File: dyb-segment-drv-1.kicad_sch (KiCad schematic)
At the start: 0 parts

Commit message: schem: add segment display
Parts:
- added U1: D168K, Display_7Segment:D1X8K, symbol Display_Character:D168K
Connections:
- new net: U1.3 (CA), U1.8 (CA)
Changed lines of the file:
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@@
 	(generator_version "10.0")
 	(paper "A4")
+	(symbol
+		(lib_id "Display_Character:D168K")
+		(at 48.26 45.72 0)
+		(unit 1)
+		(body_style 1)
+		(exclude_from_sim no)
+		(in_bom yes)
+		(on_board yes)
+		(in_pos_files yes)
+		(dnp no)
+		(fields_autoplaced yes)
+		(property "Reference" "U1"
+			(at 48.26 27.94 0)
+			(show_name no)
+			(do_not_autoplace no)
+			(effects
+				(font
+					(size 1.27 1.27)
+				)
+			)
+		)
+		(property "Value" "D168K"
+			(at 48.26 30.48 0)
+			(show_name no)
+			(do_not_autoplace no)
+			(effects
+				(font
+					(size 1.27 1.27)
+				)
+			)
+		)
+		(property "Footprint" "Display_7Segment:D1X8K"
+			(at 48.26 60.96 0)
+			(hide yes)
+			(show_name no)
+			(do_not_autoplace no)
+			(effects
+				(font
+					(size 1.27 1.27)
+				)
+			)
+		)
+		(property "Datasheet" "https://ia800903.us.archive.org/24/items/CTKD1x8K/Cromatek%20D168K.pdf"
+			(at 35.56 33.655 0)
+			(hide yes)
+			(show_name no)
+			(do_not_autoplace no)
+			(effects
+				(font
+					(size 1.27 1.27)
+				)
+				(justify left)
+			)
+		)
+		(property "Description" "One digit 7 segment ultra bright red LED, low current, common cathode"
+			(at 48.26 45.72 0)
+			(hide yes)
+			(show_name no)
+			(do_not_autoplace no)
+			(effects
+				(font
+					(size 1.27 1.27)
+				)
+			)
+		)
+		(pin "10"
+		)
+		(pin "9"
+		)
+		(pin "8"
+		)
+		(pin "7"
+		)
+		(pin "6"
+		)
+		(pin "1"
+		)
+		(pin "4"
+		)
+		(pin "5"
+		)
+		(pin "3"
+		)
+		(pin "2"
+		)
+		(instances
+			(project "dyb-segment-drv-1"
+				(path "/0d1f997b-7d97-47c3-85c1-1ce9346504d0"
+					(reference "U1")
+					(unit 1)
+				)
+			)
+		)
+	)
 	(sheet_instances
 		(path "/"

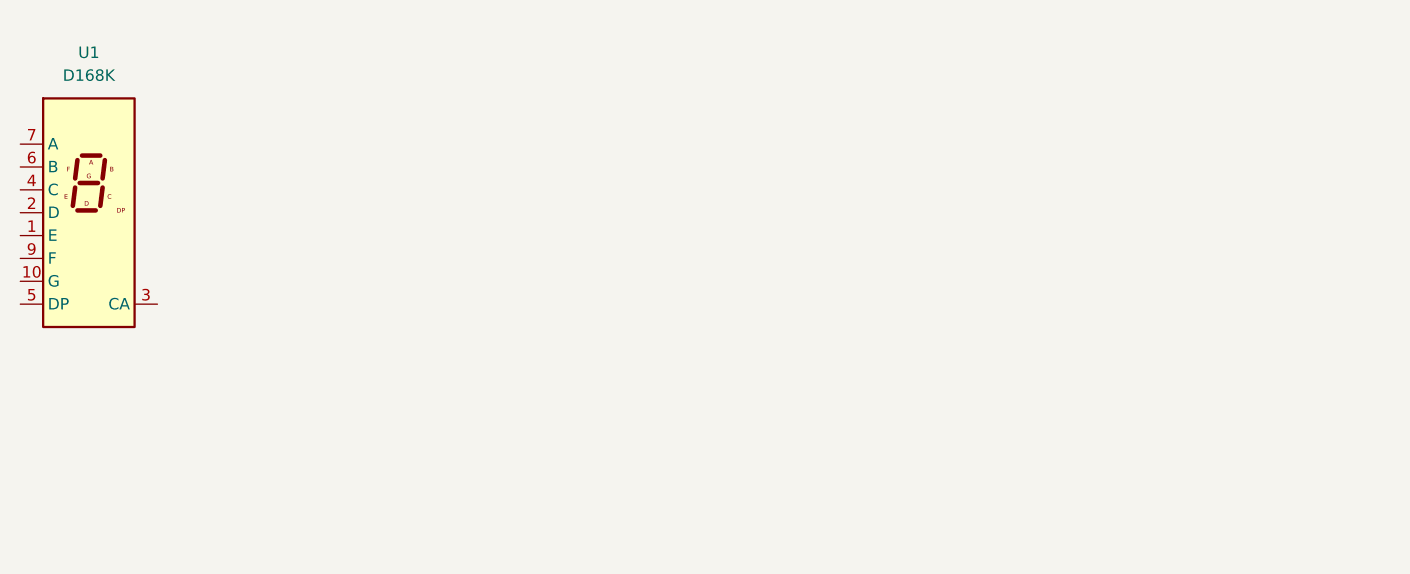
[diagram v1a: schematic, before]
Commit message: schem: add all logic gates
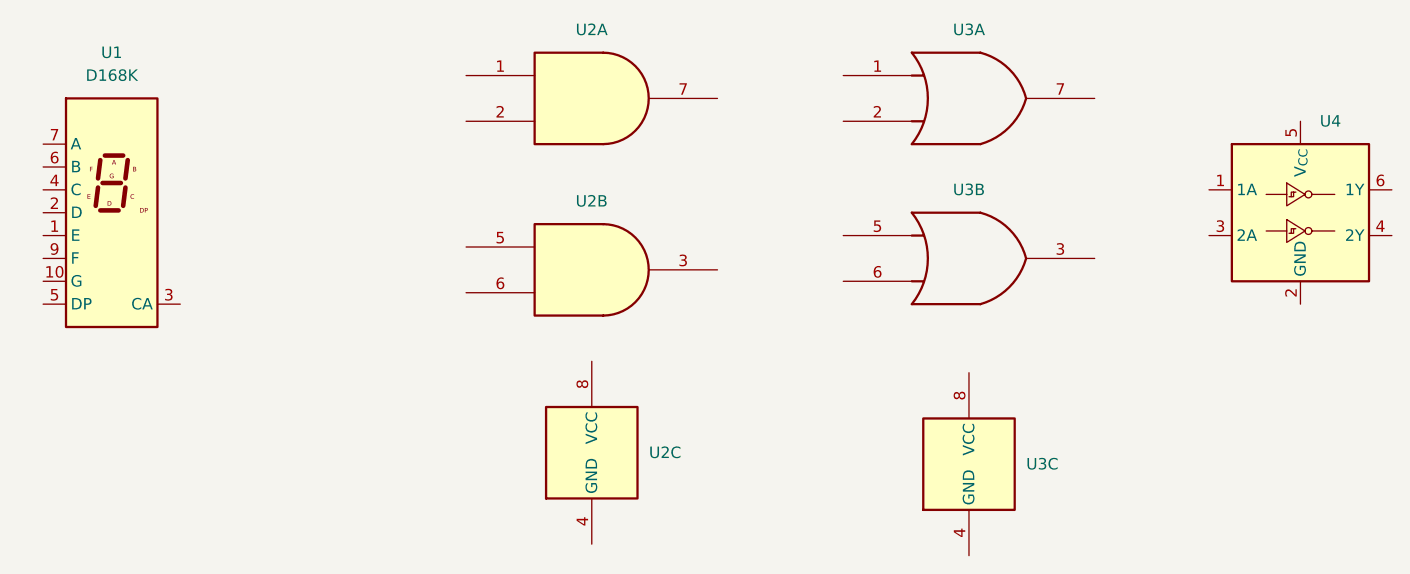
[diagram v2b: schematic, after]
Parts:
- added U2: SN74AUP2G08, Package_SO:VSSOP-8_2.3x2mm_P0.5mm, symbol GLCS:SN74AUP2G08
- added U3: 74AUC2G32, Package_DFN_QFN:QFN-20-1EP_5x5mm_P0.65mm_EP3.35x3.35mm, symbol 74xGxx:74AUC2G32
- added U4: Inverter_Schmitt_Dual, Package_TO_SOT_SMD:SOT-23-6, symbol 74xGxx:Inverter_Schmitt_Dual
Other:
- moved on the sheet: U1

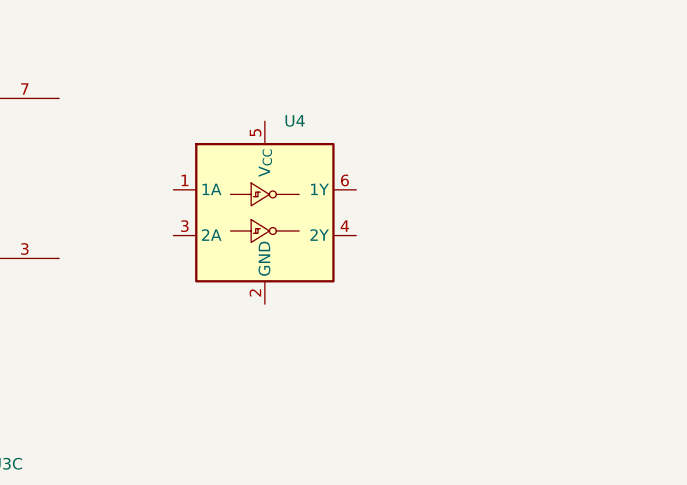
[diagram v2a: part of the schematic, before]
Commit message: schem: add mosfet
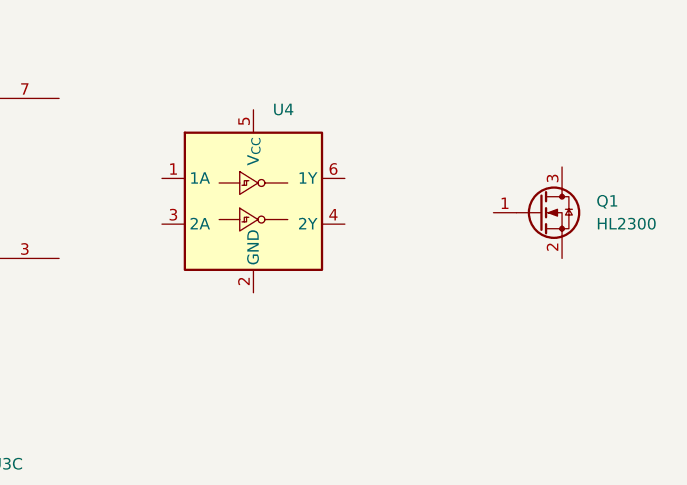
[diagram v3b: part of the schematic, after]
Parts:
- added Q1: HL2300, Package_TO_SOT_SMD:SOT-23, symbol Transistor_FET:DMN24H11DS
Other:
- moved on the sheet: U4
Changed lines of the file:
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@@
 	(symbol
 		(lib_id "74xGxx:Inverter_Schmitt_Dual")
-		(at 182.88 45.72 0)
+		(at 181.61 44.45 0)
 		(unit 1)
 		(body_style 1)
@@
 		(fields_autoplaced yes)
 		(property "Reference" "U4"
-			(at 185.0233 35.56 0)
+			(at 183.7533 34.29 0)
 			(show_name no)
 			(do_not_autoplace no)
@@
 		)
 		(property "Value" "Inverter_Schmitt_Dual"
-			(at 185.0233 35.56 0)
+			(at 183.7533 34.29 0)
 			(hide yes)
 			(show_name no)
@@
 		)
 		(property "Footprint" "Package_TO_SOT_SMD:SOT-23-6"
-			(at 182.88 45.72 0)
+			(at 181.61 44.45 0)
 			(hide yes)
 			(show_name no)
@@
 		)
 		(property "Datasheet" ""
-			(at 182.88 45.72 0)
+			(at 181.61 44.45 0)
 			(hide yes)
 			(show_name no)
@@
 		)
 		(property "Description" "Dual schmitt inverter"
-			(at 182.88 45.72 0)
+			(at 181.61 44.45 0)
 			(hide yes)
 			(show_name no)
@@
 					(unit 1)
 				)
+			)
+		)
+	)
+	(symbol
+		(lib_id "Transistor_FET:DMN24H11DS")
+		(at 213.36 45.72 0)
+		(unit 1)
+		(body_style 1)
+		(exclude_from_sim no)
+		(in_bom yes)
+		(on_board yes)
+		(in_pos_files yes)
+		(dnp no)
+		(fields_autoplaced yes)
+		(property "Reference" "Q1"
+			(at 219.71 44.4499 0)
+			(show_name no)
+			(do_not_autoplace no)
+			(effects
+				(font
+					(size 1.27 1.27)
+				)
+				(justify left)
+			)
+		)
+		(property "Value" "HL2300"
+			(at 219.71 46.9899 0)
+			(show_name no)
+			(do_not_autoplace no)
+			(effects
+				(font
+					(size 1.27 1.27)
+				)
+				(justify left)
+			)
+		)
+		(property "Footprint" "Package_TO_SOT_SMD:SOT-23"
+			(at 218.44 47.625 0)
+			(hide yes)
+			(show_name no)
+			(do_not_autoplace no)
+			(effects
+				(font
+					(size 1.27 1.27)
+					(italic yes)
+				)
+				(justify left)
+			)
+		)
+		(property "Datasheet" "http://www.diodes.com/assets/Datasheets/DMN24H11DS.pdf"
+			(at 218.44 49.53 0)
+			(hide yes)
+			(show_name no)
+			(do_not_autoplace no)
+			(effects
+				(font
+					(size 1.27 1.27)
+				)
+				(justify left)
+			)
+		)
+		(property "Description" "0.27A Id, 240V Vds, N-Channel MOSFET, SOT-23"
+			(at 213.36 45.72 0)
+			(hide yes)
+			(show_name no)
+			(do_not_autoplace no)
+			(effects
+				(font
+					(size 1.27 1.27)
+				)
+			)
+		)
+		(pin "1"
+		)
+		(pin "3"
+		)
+		(pin "2"
+		)
+		(instances
+			(project "dyb-segment-drv-1"
+				(path "/0d1f997b-7d97-47c3-85c1-1ce9346504d0"
+					(reference "Q1")
+					(unit 1)
+				)

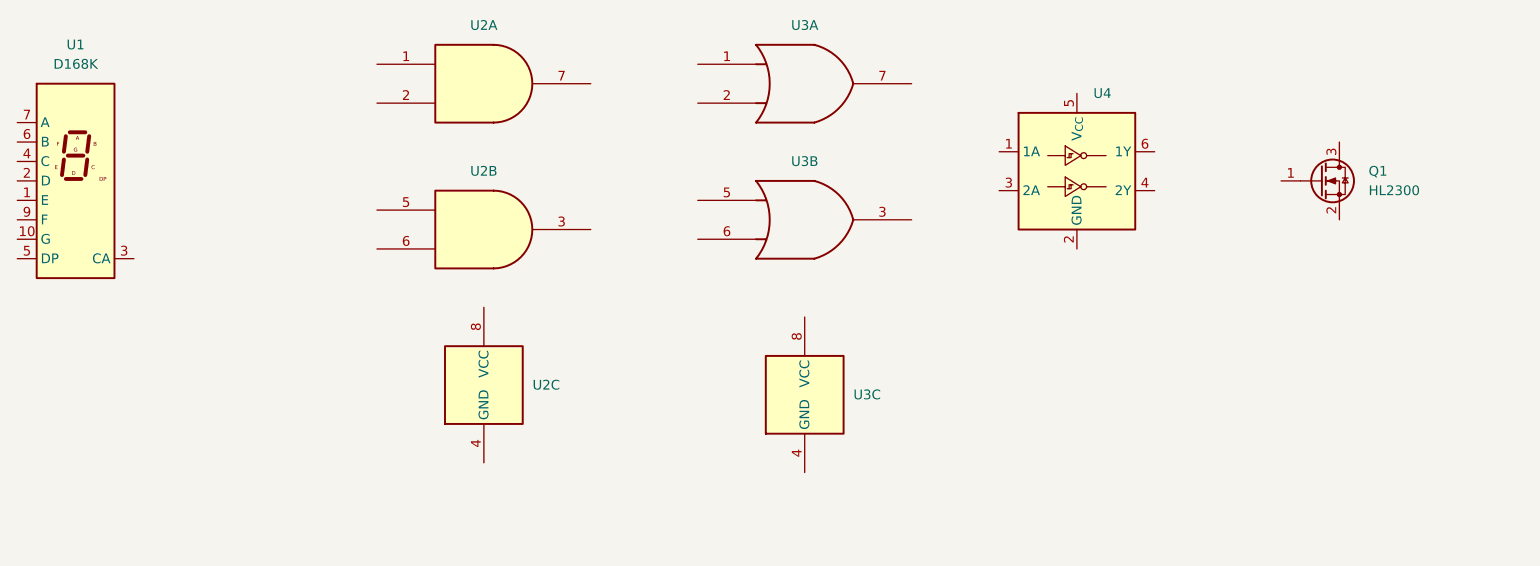
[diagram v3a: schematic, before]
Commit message: schem: add led drivers
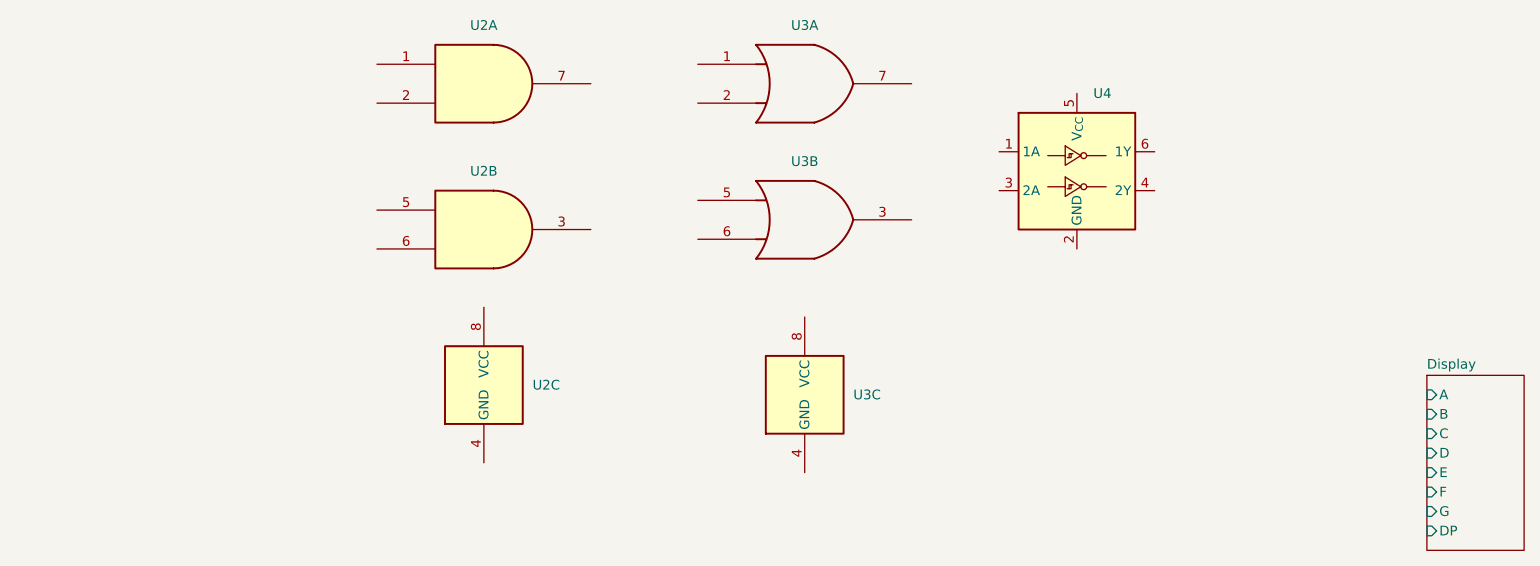
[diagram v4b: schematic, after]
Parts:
- removed Q1: HL2300, Package_TO_SOT_SMD:SOT-23, symbol Transistor_FET:DMN24H11DS
- removed U1: D168K, Display_7Segment:D1X8K, symbol Display_Character:D168K
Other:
- added sheet Display (display.kicad_sch)
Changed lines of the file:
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@@
-	)
-	(symbol
-		(lib_id "Display_Character:D168K")
-		(at 50.8 45.72 0)
-		(unit 1)
-		(body_style 1)
-		(exclude_from_sim no)
-		(in_bom yes)
-		(on_board yes)
-		(in_pos_files yes)
-		(dnp no)
-		(fields_autoplaced yes)
-		(property "Reference" "U1"
-			(at 50.8 27.94 0)
-			(show_name no)
-			(do_not_autoplace no)
-			(effects
-				(font
-					(size 1.27 1.27)
-				)
-			)
-		)
-		(property "Value" "D168K"
-			(at 50.8 30.48 0)
-			(show_name no)
-			(do_not_autoplace no)
-			(effects
-				(font
-					(size 1.27 1.27)
-				)
-			)
-		)
-		(property "Footprint" "Display_7Segment:D1X8K"
-			(at 50.8 60.96 0)
-			(hide yes)
-			(show_name no)
-			(do_not_autoplace no)
-			(effects
-				(font
-					(size 1.27 1.27)
-				)
-			)
-		)
-		(property "Datasheet" "https://ia800903.us.archive.org/24/items/CTKD1x8K/Cromatek%20D168K.pdf"
-			(at 38.1 33.655 0)
-			(hide yes)
-			(show_name no)
-			(do_not_autoplace no)
-			(effects
-				(font
-					(size 1.27 1.27)
-				)
-				(justify left)
-			)
-		)
-		(property "Description" "One digit 7 segment ultra bright red LED, low current, common cathode"
-			(at 50.8 45.72 0)
-			(hide yes)
-			(show_name no)
-			(do_not_autoplace no)
-			(effects
-				(font
-					(size 1.27 1.27)
-				)
-			)
-		)
-		(pin "10"
-		)
-		(pin "9"
-		)
-		(pin "8"
-		)
-		(pin "7"
-		)
-		(pin "6"
-		)
-		(pin "1"
-		)
-		(pin "4"
-		)
-		(pin "5"
-		)
-		(pin "3"
-		)
-		(pin "2"
-		)
-		(instances
-			(project "dyb-segment-drv-1"
-				(path "/0d1f997b-7d97-47c3-85c1-1ce9346504d0"
-					(reference "U1")
-					(unit 1)
-				)
-			)
-		)
 	)
 	(symbol
@@
 	)
 	(symbol
-		(lib_id "Transistor_FET:DMN24H11DS")
-		(at 213.36 45.72 0)
-		(unit 1)
-		(body_style 1)
-		(exclude_from_sim no)
-		(in_bom yes)
-		(on_board yes)
-		(in_pos_files yes)
-		(dnp no)
-		(fields_autoplaced yes)
-		(property "Reference" "Q1"
-			(at 219.71 44.4499 0)
-			(show_name no)
-			(do_not_autoplace no)
-			(effects
-				(font
-					(size 1.27 1.27)
-				)
-				(justify left)
-			)
-		)
-		(property "Value" "HL2300"
-			(at 219.71 46.9899 0)
-			(show_name no)
-			(do_not_autoplace no)
-			(effects
-				(font
-					(size 1.27 1.27)
-				)
-				(justify left)
-			)
-		)
-		(property "Footprint" "Package_TO_SOT_SMD:SOT-23"
-			(at 218.44 47.625 0)
-			(hide yes)
-			(show_name no)
-			(do_not_autoplace no)
-			(effects
-				(font
-					(size 1.27 1.27)
-					(italic yes)
-				)
-				(justify left)
-			)
-		)
-		(property "Datasheet" "http://www.diodes.com/assets/Datasheets/DMN24H11DS.pdf"
-			(at 218.44 49.53 0)
-			(hide yes)
-			(show_name no)
-			(do_not_autoplace no)
-			(effects
-				(font
-					(size 1.27 1.27)
-				)
-				(justify left)
-			)
-		)
-		(property "Description" "0.27A Id, 240V Vds, N-Channel MOSFET, SOT-23"
-			(at 213.36 45.72 0)
-			(hide yes)
-			(show_name no)
-			(do_not_autoplace no)
-			(effects
-				(font
-					(size 1.27 1.27)
-				)
-			)
-		)
-		(pin "1"
-		)
-		(pin "3"
-		)
-		(pin "2"
-		)
-		(instances
-			(project "dyb-segment-drv-1"
-				(path "/0d1f997b-7d97-47c3-85c1-1ce9346504d0"
-					(reference "Q1")
-					(unit 1)
-				)
-			)
-		)
-	)
-	(symbol
 		(lib_id "GLCS:SN74AUP2G08")
 		(at 105.41 52.07 0)
@@
 				)
 			)
+		)
+	)
+	(sheet
+		(at 227.33 71.12)
+		(size 12.7 22.86)
+		(exclude_from_sim no)
+		(in_bom yes)
+		(on_board yes)
+		(dnp no)
+		(fields_autoplaced yes)
+		(stroke
+			(width 0.1524)
+			(type solid)
+		)
+		(fill
+			(color 0 0 0 0)
+		)
+		(property "Sheetname" "Display"
+			(at 227.33 70.4084 0)
+			(show_name no)
+			(do_not_autoplace no)
+			(effects
+				(font
+					(size 1.27 1.27)
+				)
+				(justify left bottom)
+			)
+		)
+		(property "Sheetfile" "display.kicad_sch"
+			(at 227.33 94.5646 0)
+			(hide yes)
+			(show_name no)
+			(do_not_autoplace no)
+			(effects
+				(font
+					(size 1.27 1.27)
+				)
+				(justify left top)
+			)
+		)
+		(pin "B" input
+			(at 227.33 76.2 180)
+			(effects
+				(font
+					(size 1.27 1.27)
+				)
+				(justify left)
+			)
+		)
+		(pin "A" input
+			(at 227.33 73.66 180)
+			(effects
+				(font
+					(size 1.27 1.27)
+				)
+				(justify left)
+			)
+		)
+		(pin "E" input
+			(at 227.33 83.82 180)
+			(effects
+				(font
+					(size 1.27 1.27)
+				)
+				(justify left)
+			)
+		)
+		(pin "C" input
+			(at 227.33 78.74 180)
+			(effects
+				(font
+					(size 1.27 1.27)
+				)
+				(justify left)
+			)
+		)
+		(pin "G" input
+			(at 227.33 88.9 180)
+			(effects
+				(font
+					(size 1.27 1.27)
+				)
+				(justify left)
+			)
+		)
+		(pin "F" input
+			(at 227.33 86.36 180)
+			(effects
+				(font
+					(size 1.27 1.27)
+				)
+				(justify left)
+			)
+		)
+		(pin "DP" input
+			(at 227.33 91.44 180)
+			(effects
+				(font
+					(size 1.27 1.27)
+				)
+				(justify left)
+			)
+		)
+		(pin "D" input
+			(at 227.33 81.28 180)
+			(effects
+				(font
+					(size 1.27 1.27)
+				)
+				(justify left)
+			)
+		)
+		(instances
+			(project "dyb-segment-drv-1"
+				(path "/0d1f997b-7d97-47c3-85c1-1ce9346504d0"
+					(page "2")
+				)
+			)
